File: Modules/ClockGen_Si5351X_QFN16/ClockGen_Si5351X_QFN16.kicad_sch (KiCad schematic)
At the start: 111 parts, among them J1 Screw Terminal, J10 2.54mm Stackable Socket, J11 2.54mm Stackable Socket, J12 2.54mm Stackable Socket, J13 2.54mm Stackable Socket, J14 2.54mm Stackable Socket, J2 JST SH, J3 SMA, J4 2.54 Pins, J5 2.54 Pins, J6 SMA, J7 SMA, J8 SMA, J9 SMA, Q1 GSFJ0300, Q2 GSFJ0300, SW1 SW_SPDT, U1 NCV68061, U2 NCV68061, U3 TPS7E8201, U4 SI5351B-B-GM1, U5 AP2127K-ADJ, U6 LM66200, Y1 25MHz

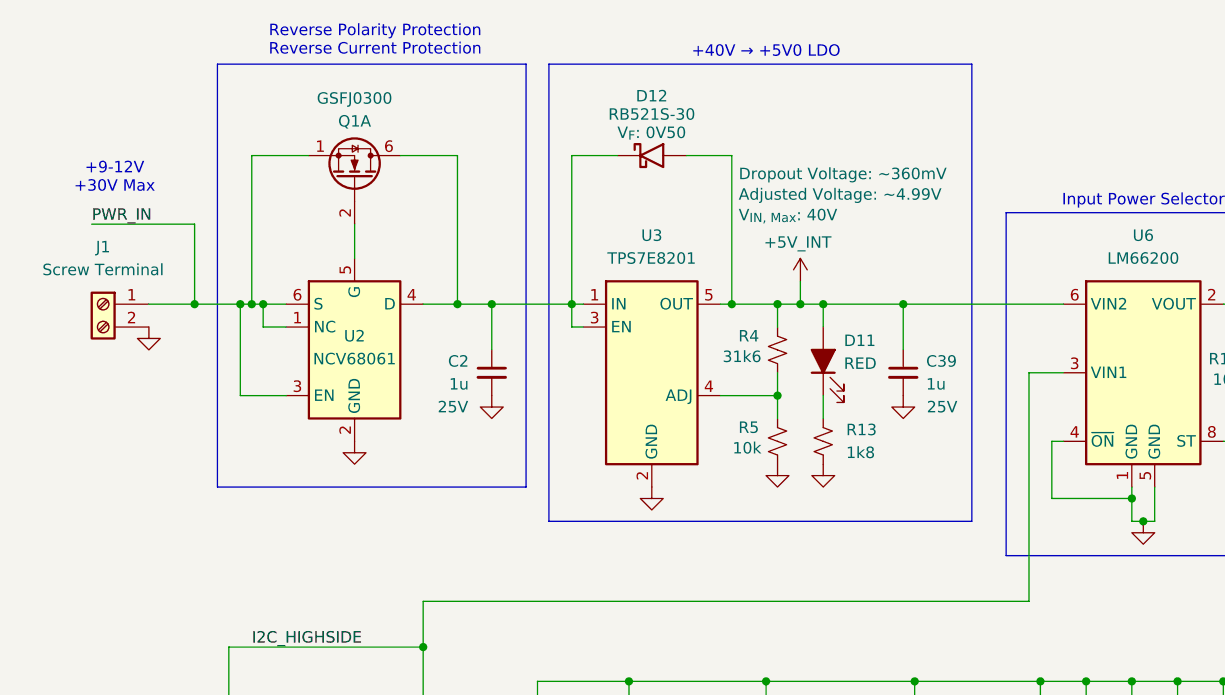
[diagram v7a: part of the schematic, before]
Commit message: Added input power snubber
Just in case :P
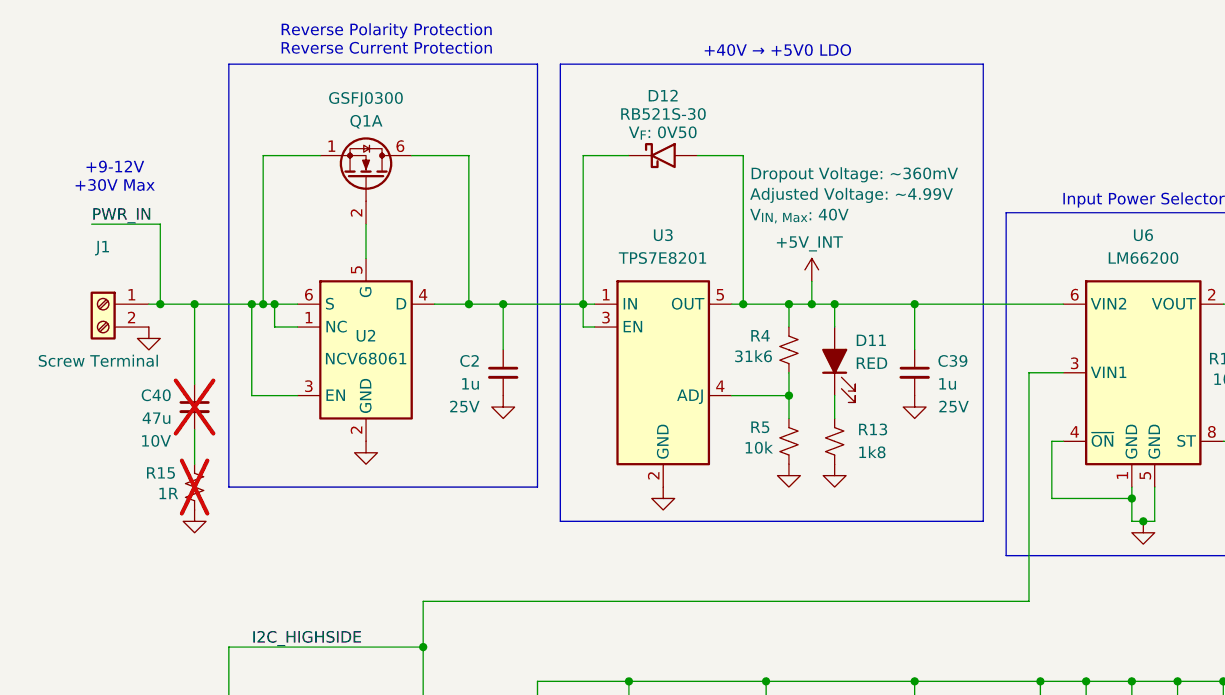
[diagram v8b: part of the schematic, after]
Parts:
- added C40: 47u, libraries:Worthington_C_0805, symbol Device:C_Small
- added R15: 1R, Resistor_SMD:R_0805_2012Metric, symbol Device:R_Small_US
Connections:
- net GND: now also R15.1
- net PWR_IN: now also C40.1
- new net: C40.2, R15.2
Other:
- moved on the sheet: C2, C39, D11, D12, Q1A, R13, R4, R5, U2, U3
